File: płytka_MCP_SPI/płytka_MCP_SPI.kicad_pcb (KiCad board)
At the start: 2 copper layers, 77.3 x 77 mm, 29 parts, among them J1 A0, J10 V0, J11 Ext, J13 U2, J15 U2, J16 U3, J17 RS, J18 K, J19 A, J2 A1, J20 VDD, J21 GND, J23 VSS, J24 Conn_01x16_Pin, J25 LCD, J26 VCC, J27 SPI, J3 A2, J6 INTA, J7 INTB, J8 INTA, J9 RESET, U1 MCP23S17_SP

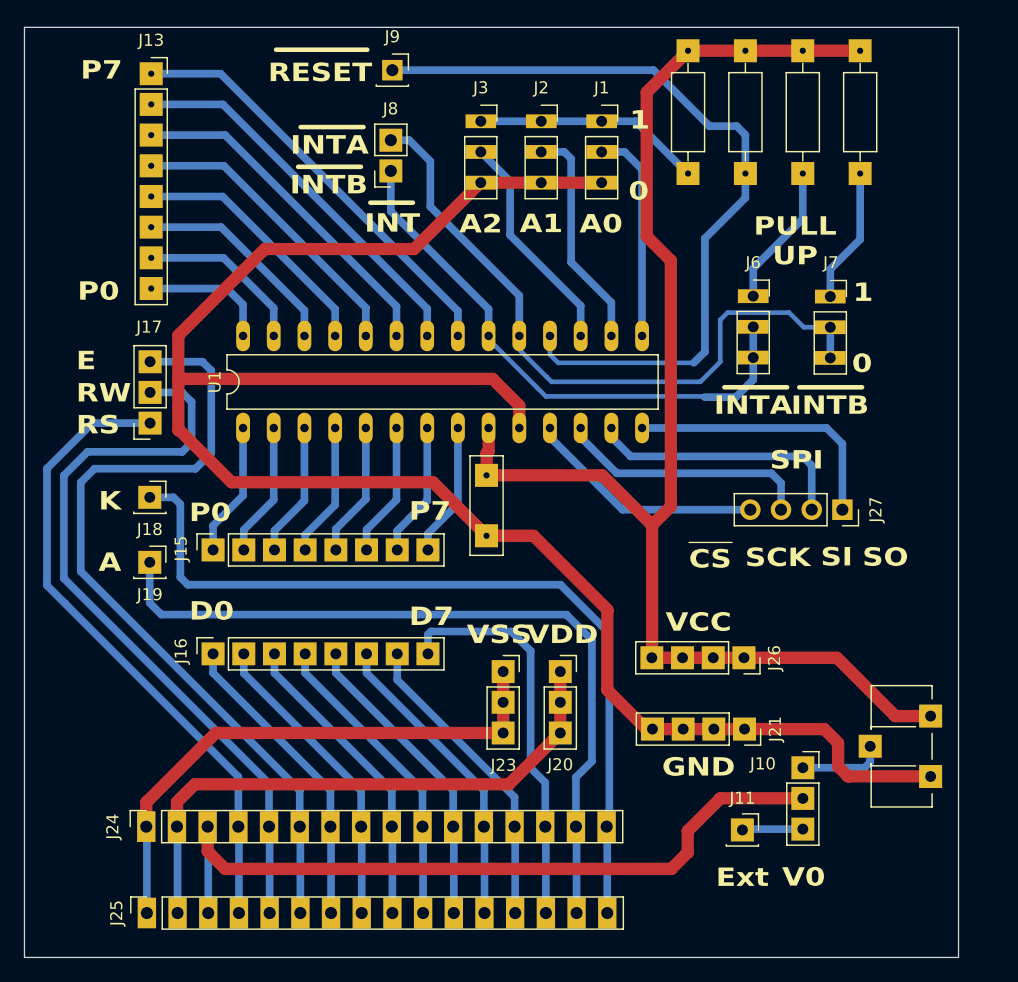
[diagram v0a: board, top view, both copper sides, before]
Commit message: Korekcja rozmiaru płytki, utworzenie draftow, do druku
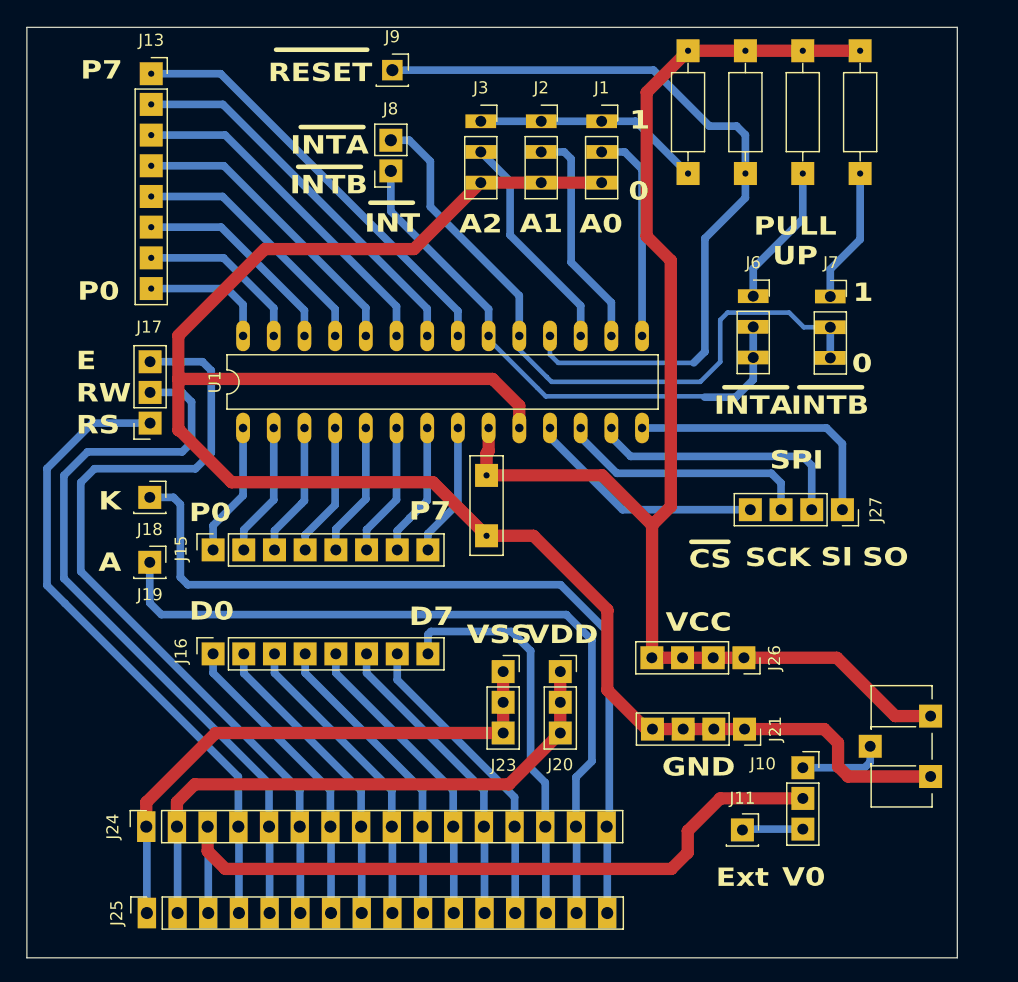
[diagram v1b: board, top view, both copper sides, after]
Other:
- board size 77.3 x 77 mm -> 77 x 77 mm
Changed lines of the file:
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@@
 			(at 0 10.39 90)
 			(layer "F.Fab")
+			(hide yes)
 			(effects
 				(font
@@
 		(pad "1" thru_hole rect
 			(at 0 0 270)
-			(size 1.7 1.7)
-			(drill 1)
+			(size 1.905 1.905)
+			(drill 0.9)
 			(layers "*.Cu" "*.Mask")
 			(remove_unused_layers no)
@@
 			(pintype "passive")
 		)
-		(pad "2" thru_hole circle
+		(pad "2" thru_hole rect
 			(at 0 2.54 270)
-			(size 1.7 1.7)
-			(drill 1)
+			(size 1.905 1.905)
+			(drill 0.9)
 			(layers "*.Cu" "*.Mask")
 			(remove_unused_layers no)
@@
 			(pinfunction "Pin_2")
 			(pintype "passive")
+			(thermal_bridge_angle 45)
 		)
-		(pad "3" thru_hole circle
+		(pad "3" thru_hole rect
 			(at 0 5.08 270)
-			(size 1.7 1.7)
-			(drill 1)
+			(size 1.905 1.905)
+			(drill 0.9)
 			(layers "*.Cu" "*.Mask")
 			(remove_unused_layers no)
@@
 			(pinfunction "Pin_3")
 			(pintype "passive")
+			(thermal_bridge_angle 45)
 		)
-		(pad "4" thru_hole circle
+		(pad "4" thru_hole rect
 			(at 0 7.62 270)
-			(size 1.7 1.7)
-			(drill 1)
+			(size 1.905 1.905)
+			(drill 0.9)
 			(layers "*.Cu" "*.Mask")
 			(remove_unused_layers no)
@@
 			(pinfunction "Pin_4")
 			(pintype "passive")
+			(thermal_bridge_angle 45)
 		)
 		(embedded_fonts no)
@@
 	)
 	(gr_line
-		(start 106.460333 80.98)
-		(end 110.020333 80.98)
+		(start 106.65 80.93)
+		(end 109.72 80.93)
 		(stroke
-			(width 0.1)
-			(type default)
+			(width 0.381)
+			(type solid)
 		)
 		(layer "F.SilkS")
@@
 	)
 	(gr_rect
-		(start 51.46 38.355)
-		(end 128.76 115.325)
+		(start 51.66 38.355)
+		(end 128.66 115.355)
 		(stroke
 			(width 0.05)
@@
 		(layer "Dwgs.User")
 		(pts
-			(xy 133.54544 109.89) (xy 133.54544 145.89)
+			(xy 51.66 38.355) (xy 128.66 38.355)
 		)
-		(height 5.60456)
-		(orientation 1)
+		(height -7.155)
+		(orientation 0)
 		(format
 			(prefix "")
@@
 			(keep_text_aligned yes)
 		)
-		(gr_text "36"
-			(at 138 127.89 90)
+		(gr_text "77"
+			(at 90.16 30.05 0)
 			(layer "Dwgs.User")
 			(effects
@@
 		(layer "Dwgs.User")
 		(pts
-			(xy 51.54 169.89) (xy 149.54 169.89)
+			(xy 128.66 115.355) (xy 128.66 38.355)
 		)
-		(height 4.96)
-		(orientation 0)
+		(height 3.61)
+		(orientation 1)
 		(format
 			(prefix "")
@@
 			(keep_text_aligned yes)
 		)
-		(gr_text "98"
-			(at 100.54 173.7 0)
+		(gr_text "77"
+			(at 131.12 76.855 90)
 			(layer "Dwgs.User")
 			(effects
@@
 		(layer "Dwgs.User")
 		(pts
-			(xy 128.76 38.355) (xy 128.76 115.325)
+			(xy 133.54544 109.89) (xy 133.54544 145.89)
 		)
-		(height 33.51)
+		(height 5.60456)
 		(orientation 1)
 		(format
@@
 			(keep_text_aligned yes)
 		)
-		(gr_text "76,97"
-			(at 161.12 76.84 90)
+		(gr_text "36"
+			(at 138 127.89 90)
 			(layer "Dwgs.User")
 			(effects
@@
 		(layer "Dwgs.User")
 		(pts
-			(xy 149.54 169.89) (xy 149.54 109.89)
+			(xy 51.54 169.89) (xy 149.54 169.89)
 		)
-		(height 8.31)
-		(orientation 1)
+		(height 4.96)
+		(orientation 0)
 		(format
 			(prefix "")
@@
 			(keep_text_aligned yes)
 		)
-		(gr_text "60"
-			(at 156.7 139.89 90)
+		(gr_text "98"
+			(at 100.54 173.7 0)
 			(layer "Dwgs.User")
 			(effects
@@
 		(layer "Dwgs.User")
 		(pts
-			(xy 51.46 38.355) (xy 128.76 38.355)
+			(xy 149.54 169.89) (xy 149.54 109.89)
 		)
-		(height -11.015)
-		(orientation 0)
+		(height 8.31)
+		(orientation 1)
 		(format
 			(prefix "")
@@
 			(keep_text_aligned yes)
 		)
-		(gr_text "77,3"
-			(at 90.11 26.19 0)
+		(gr_text "60"
+			(at 156.7 139.89 90)
 			(layer "Dwgs.User")
 			(effects
@@
 	)
 	(group ""
-		(members "acd6a382-df3b-436c-a1a8-3759a3338cc9")
+		(members "1092fc1a-5df2-4544-83e0-d84b64546b13" "4b902779-8af4-4a5e-83f4-d6a086befd7d")
 	)
 	(group ""
-		(members "ae3650fa-d5b3-4dfb-b49b-eb3c415f8550")
+		(members "acd6a382-df3b-436c-a1a8-3759a3338cc9")
 	)
 	(group ""
-		(members "1092fc1a-5df2-4544-83e0-d84b64546b13" "4b902779-8af4-4a5e-83f4-d6a086befd7d")
+		(members "ae3650fa-d5b3-4dfb-b49b-eb3c415f8550")
 	)
 	(group ""

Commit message: Normalizacja wielkosci plytke
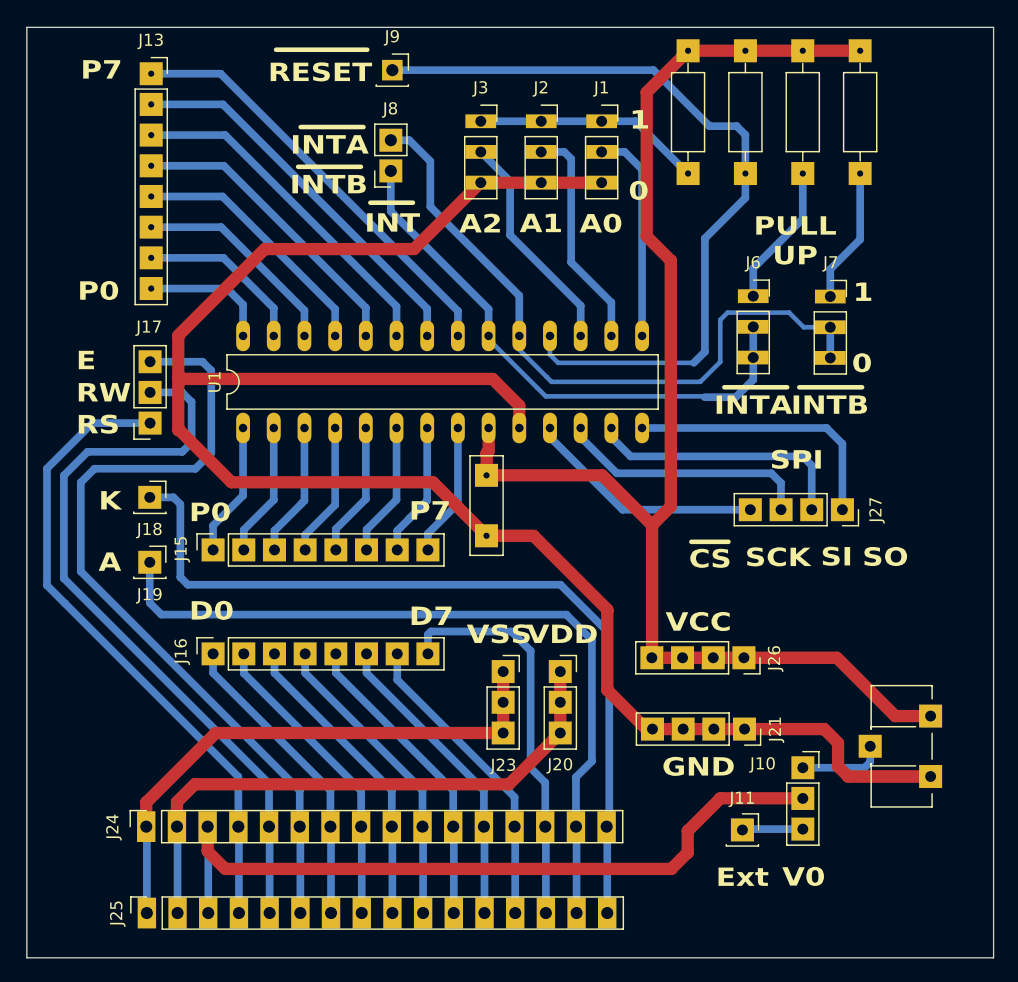
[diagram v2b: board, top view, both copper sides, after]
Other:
- board size 77 x 77 mm -> 80 x 77 mm
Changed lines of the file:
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@@
 	(gr_rect
 		(start 51.66 38.355)
-		(end 128.66 115.355)
+		(end 131.66 115.355)
 		(stroke
 			(width 0.05)
@@
 		(gr_text "80,0000 mm"
 			(at 93.57 150.086 0)
-			(layer "Dwgs.User")
-			(effects
-				(font
-					(size 1 1)
-					(thickness 0.15)
-				)
-			)
-		)
-	)
-	(dimension
-		(type orthogonal)
-		(layer "Dwgs.User")
-		(pts
-			(xy 51.66 38.355) (xy 128.66 38.355)
-		)
-		(height -7.155)
-		(orientation 0)
-		(format
-			(prefix "")
-			(suffix "")
-			(units 3)
-			(units_format 0)
-			(precision 4)
-			(suppress_zeroes yes)
-		)
-		(style
-			(thickness 0.1)
-			(arrow_length 1.27)
-			(text_position_mode 0)
-			(arrow_direction outward)
-			(extension_height 0.58642)
-			(extension_offset 0.5)
-			(keep_text_aligned yes)
-		)
-		(gr_text "77"
-			(at 90.16 30.05 0)
-			(layer "Dwgs.User")
-			(effects
-				(font
-					(size 1 1)
-					(thickness 0.15)
-				)
-			)
-		)
-	)
-	(dimension
-		(type orthogonal)
-		(layer "Dwgs.User")
-		(pts
-			(xy 128.66 115.355) (xy 128.66 38.355)
-		)
-		(height 3.61)
-		(orientation 1)
-		(format
-			(prefix "")
-			(suffix "")
-			(units 3)
-			(units_format 0)
-			(precision 4)
-			(suppress_zeroes yes)
-		)
-		(style
-			(thickness 0.1)
-			(arrow_length 1.27)
-			(text_position_mode 0)
-			(arrow_direction outward)
-			(extension_height 0.58642)
-			(extension_offset 0.5)
-			(keep_text_aligned yes)
-		)
-		(gr_text "77"
-			(at 131.12 76.855 90)
 			(layer "Dwgs.User")
 			(effects
@@
 			(layer "Dwgs.User")
 			(effects
+				(font
+					(size 1 1)
+					(thickness 0.15)
+				)
+			)
+		)
+	)
+	(dimension
+		(type orthogonal)
+		(layer "Dwgs.User")
+		(pts
+			(xy 131.66 38.355) (xy 131.66 115.355)
+		)
+		(height 4.34)
+		(orientation 1)
+		(format
+			(prefix "")
+			(suffix "")
+			(units 3)
+			(units_format 0)
+			(precision 4)
+			(suppress_zeroes yes)
+		)
+		(style
+			(thickness 0.1)
+			(arrow_length 1.27)
+			(text_position_mode 0)
+			(arrow_direction outward)
+			(extension_height 0.58642)
+			(extension_offset 0.5)
+			(keep_text_aligned yes)
+		)
+		(gr_text "77"
+			(at 134.85 76.855 90)
+			(layer "Dwgs.User")
+			(effects
+				(font
+					(size 1 1)
+					(thickness 0.15)
+				)
+			)
+		)
+	)
+	(dimension
+		(type orthogonal)
+		(layer "Dwgs.User")
+		(pts
+			(xy 51.66 38.355) (xy 131.66 38.355)
+		)
+		(height -4.355)
+		(orientation 0)
+		(format
+			(prefix "")
+			(suffix "")
+			(units 3)
+			(units_format 0)
+			(precision 4)
+			(suppress_zeroes yes)
+		)
+		(style
+			(thickness 0.1)
+			(arrow_length 1.27)
+			(text_position_mode 0)
+			(arrow_direction outward)
+			(extension_height 0.58642)
+			(extension_offset 0.5)
+			(keep_text_aligned yes)
+		)
+		(gr_text "80"
+			(at 91.66 32.85 0)
+			(layer "Dwgs.User")
+			(effects

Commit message: Wyrownane otwory
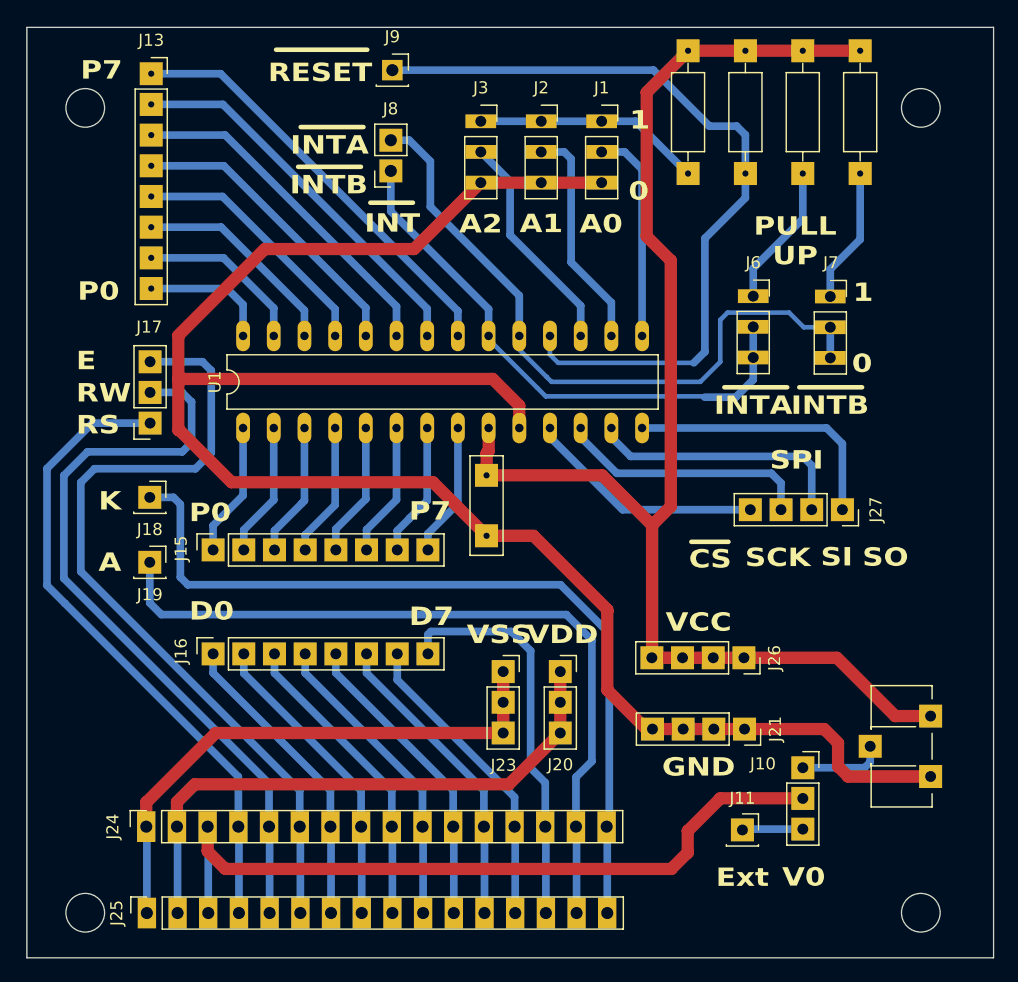
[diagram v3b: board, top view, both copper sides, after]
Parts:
- added ?: , , F.Cu at (125.6, 111.6)
- added ?: , , F.Cu at (56.5, 45.0)
- added ?: , , F.Cu at (125.6, 45.0)
- added ?: , , F.Cu at (56.5, 111.6)
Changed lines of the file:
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@@
 		)
 	)
+	(footprint ""
+		(layer "F.Cu")
+		(at 125.64 111.625)
+		(property "Reference" ""
+			(at 0 0 0)
+			(layer "F.SilkS")
+			(effects
+				(font
+					(size 1.27 1.27)
+					(thickness 0.15)
+				)
+			)
+		)
+		(property "Value" ""
+			(at 0 0 0)
+			(layer "F.Fab")
+			(effects
+				(font
+					(size 1.27 1.27)
+					(thickness 0.15)
+				)
+			)
+		)
+		(property "Datasheet" ""
+			(at 0 0 0)
+			(layer "F.Fab")
+			(hide yes)
+			(effects
+				(font
+					(size 1.27 1.27)
+					(thickness 0.15)
+				)
+			)
+		)
+		(property "Description" ""
+			(at 0 0 0)
+			(layer "F.Fab")
+			(hide yes)
+			(effects
+				(font
+					(size 1.27 1.27)
+					(thickness 0.15)
+				)
+			)
+		)
+		(pad "" np_thru_hole circle
+			(at 0 0)
+			(size 3.2 3.2)
+			(drill 3.2)
+			(layers "*.Cu" "*.Mask")
+		)
+		(embedded_fonts no)
+	)
+	(footprint ""
+		(layer "F.Cu")
+		(at 56.49 45.02)
+		(property "Reference" ""
+			(at 0 0 0)
+			(layer "F.SilkS")
+			(effects
+				(font
+					(size 1.27 1.27)
+					(thickness 0.15)
+				)
+			)
+		)
+		(property "Value" ""
+			(at 0 0 0)
+			(layer "F.Fab")
+			(effects
+				(font
+					(size 1.27 1.27)
+					(thickness 0.15)
+				)
+			)
+		)
+		(property "Datasheet" ""
+			(at 0 0 0)
+			(layer "F.Fab")
+			(hide yes)
+			(effects
+				(font
+					(size 1.27 1.27)
+					(thickness 0.15)
+				)
+			)
+		)
+		(property "Description" ""
+			(at 0 0 0)
+			(layer "F.Fab")
+			(hide yes)
+			(effects
+				(font
+					(size 1.27 1.27)
+					(thickness 0.15)
+				)
+			)
+		)
+		(pad "" np_thru_hole circle
+			(at 0 0)
+			(size 3.2 3.2)
+			(drill 3.2)
+			(layers "*.Cu" "*.Mask")
+		)
+		(embedded_fonts no)
+	)
+	(footprint ""
+		(layer "F.Cu")
+		(at 125.64 45.02)
+		(property "Reference" ""
+			(at 0 0 0)
+			(layer "F.SilkS")
+			(effects
+				(font
+					(size 1.27 1.27)
+					(thickness 0.15)
+				)
+			)
+		)
+		(property "Value" ""
+			(at 0 0 0)
+			(layer "F.Fab")
+			(effects
+				(font
+					(size 1.27 1.27)
+					(thickness 0.15)
+				)
+			)
+		)
+		(property "Datasheet" ""
+			(at 0 0 0)
+			(layer "F.Fab")
+			(hide yes)
+			(effects
+				(font
+					(size 1.27 1.27)
+					(thickness 0.15)
+				)
+			)
+		)
+		(property "Description" ""
+			(at 0 0 0)
+			(layer "F.Fab")
+			(hide yes)
+			(effects
+				(font
+					(size 1.27 1.27)
+					(thickness 0.15)
+				)
+			)
+		)
+		(pad "" np_thru_hole circle
+			(at 0 0)
+			(size 3.2 3.2)
+			(drill 3.2)
+			(layers "*.Cu" "*.Mask")
+		)
+		(embedded_fonts no)
+	)
 	(footprint "Library:PinSocket_1x03_P2.54mm_Vertical"
 		(layer "F.Cu")
@@
 		)
 	)
+	(footprint ""
+		(layer "F.Cu")
+		(at 56.49 111.625)
+		(property "Reference" ""
+			(at 0 0 0)
+			(layer "F.SilkS")
+			(effects
+				(font
+					(size 1.27 1.27)
+					(thickness 0.15)
+				)
+			)
+		)
+		(property "Value" ""
+			(at 0 0 0)
+			(layer "F.Fab")
+			(effects
+				(font
+					(size 1.27 1.27)
+					(thickness 0.15)
+				)
+			)
+		)
+		(property "Datasheet" ""
+			(at 0 0 0)
+			(layer "F.Fab")
+			(hide yes)
+			(effects
+				(font
+					(size 1.27 1.27)
+					(thickness 0.15)
+				)
+			)
+		)
+		(property "Description" ""
+			(at 0 0 0)
+			(layer "F.Fab")
+			(hide yes)
+			(effects
+				(font
+					(size 1.27 1.27)
+					(thickness 0.15)
+				)
+			)
+		)
+		(pad "" np_thru_hole circle
+			(at 0 0)
+			(size 3.2 3.2)
+			(drill 3.2)
+			(layers "*.Cu" "*.Mask")
+		)
+		(embedded_fonts no)
+	)
 	(footprint "Connector_PinSocket_2.54mm:PinSocket_1x04_P2.54mm_Vertical"
 		(layer "F.Cu")
@@
 	)
 	(gr_circle
-		(center 125.01 111.625)
-		(end 126.26 112.625)
+		(center 125.64 111.625)
+		(end 126.89 112.625)
 		(stroke
 			(width 0.1)
@@
 	)
 	(gr_circle
-		(center 125.01 45.02)
-		(end 125.41 46.57)
+		(center 125.64 45.02)
+		(end 127.240781 45.02)
 		(stroke
 			(width 0.1)
-			(type default)
+			(type solid)
 		)
 		(fill no)
